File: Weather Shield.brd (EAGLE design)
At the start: 30.5 x 35.6 mm, 40 parts, among them Q1 BSS138, Q2 BSS138, U1 DS3231SN, U4 MPL3115A2LGA8, U5 HTU21D

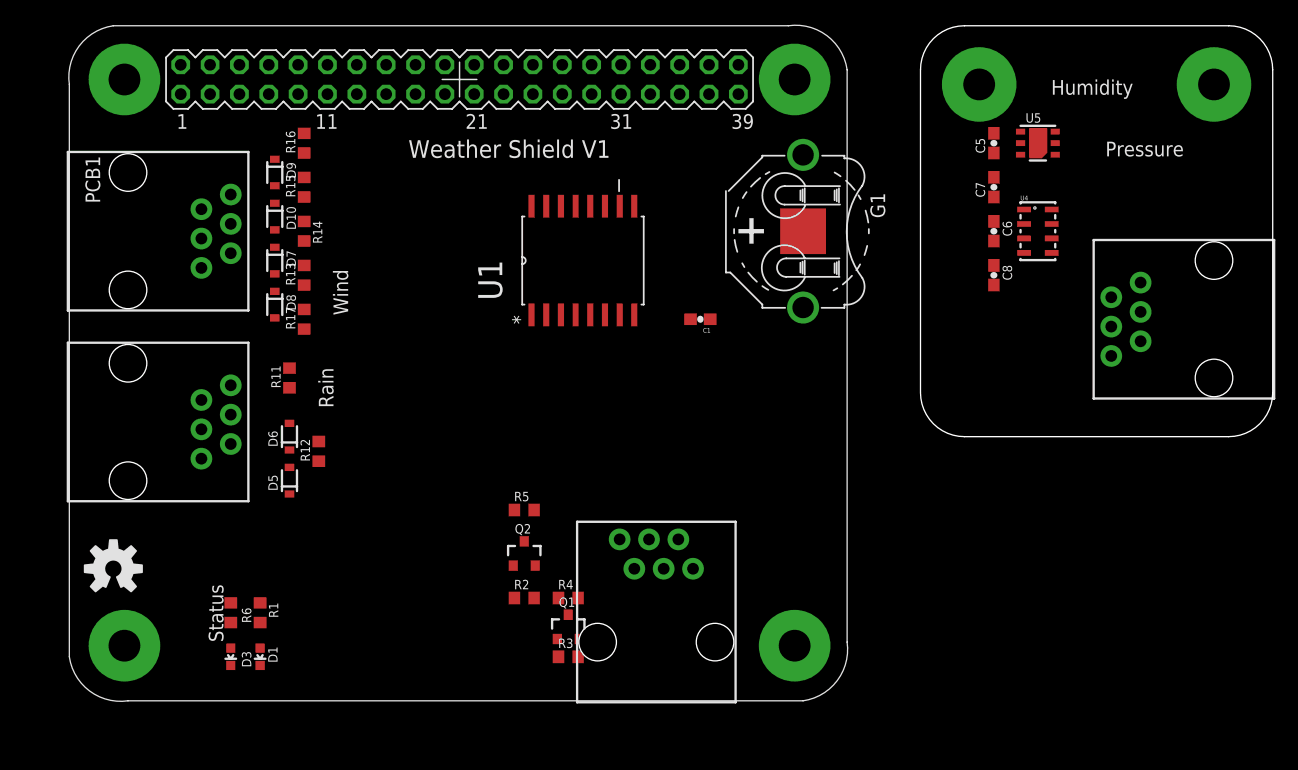
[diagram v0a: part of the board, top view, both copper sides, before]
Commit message: FSE_Weather_Shield.lbr added
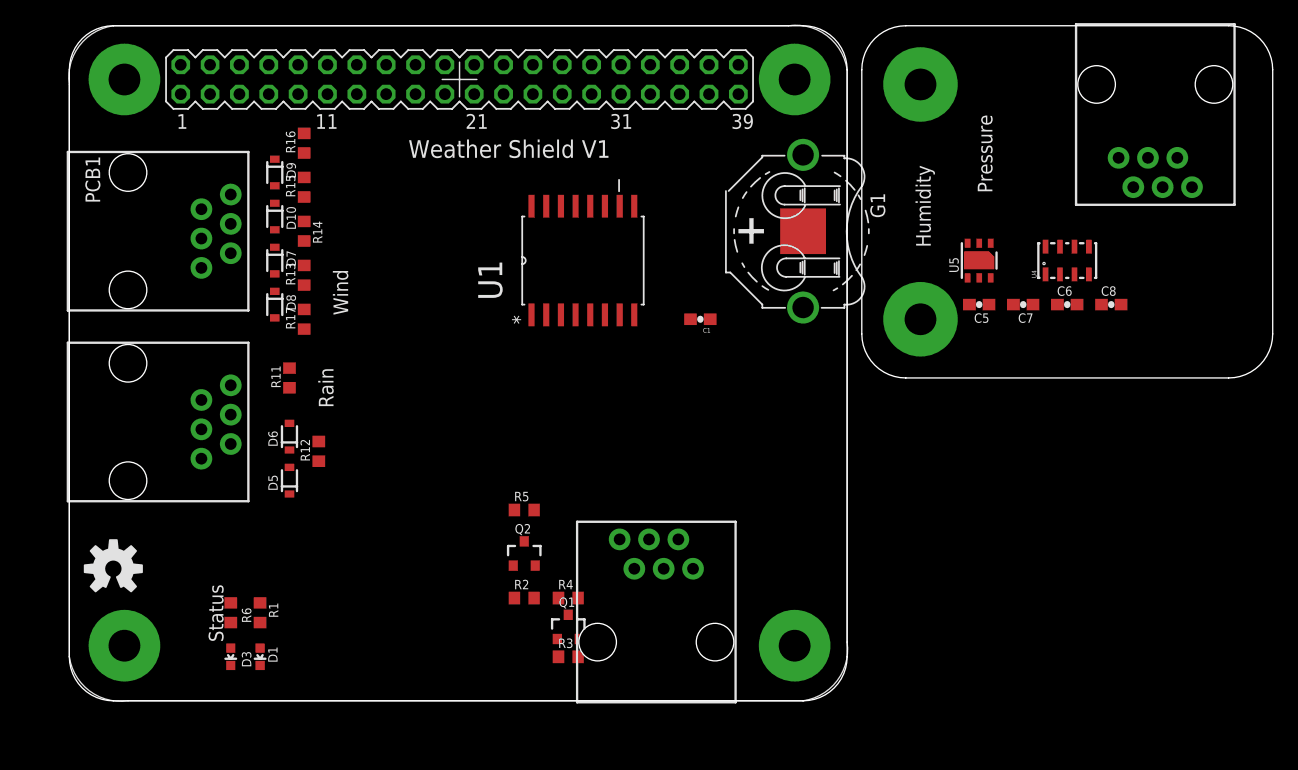
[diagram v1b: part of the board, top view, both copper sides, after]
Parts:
- moved JP9-DNP2 25.4 mm to (99.1, 53.3), turned to 180 degrees
- moved C5 14.0 mm to (78.7, 34.3), turned to 180 degrees
- moved U5 11.4 mm to (78.7, 38.1), turned to 90 degrees
- moved C7 10.5 mm to (82.5, 34.3), turned to 180 degrees
- moved C8 10.5 mm to (90.2, 34.3), turned to 0 degrees
- moved C6 8.98 mm to (86.4, 34.3), turned to 0 degrees
- moved U4 3.59 mm to (86.4, 38.1), turned to 90 degrees
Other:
- board size 30.5 x 35.6 mm -> 104.1 x 58.4 mm

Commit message: initial project version
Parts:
- added C10, C11: 1.0uF, rcl:C0603
- added C2, C9: 10uF, rcl:C0603
- added C3, C4: 47uF, SparkFun-Capacitors:EIA3528
- added D11, D4: ZLLS500, SparkFun-DiscreteSemi:SOT23
- added J7, J8: M023.5MM, SparkFun-Connectors:SCREWTERMINAL-3.5MM-2
- added JP1: (no value), SparkFun-Passives:SJ_2S
- added JP2: (no value), SparkFun-Passives:SJ_2S-NO
- added JP3: JUMPER-PTH-2-NC, SparkFun-Passives:PTH-JUMPER-NC_BOTTOM_NO_SILK
- added L1: 68uH, SparkFun-Passives:CR75
- added R10: 24k, rcl:R0603
- added R20: 220k, rcl:R0603
- added R21, R23: not fitted, rcl:R0603
- added R22: 10k, pot:S64Y
- added R8: 0.2, rcl:R0603
- added R9: 9.1k, rcl:R0603
- added TP1: SET, testpad:B1,27
- added U$1, U$2, U$3: DEAN_CONNECTOR, FSE_Weather_Shield:DEAN_CONNECTOR
- added U2: LT3652, SparkFun-PowerIC:MSOP-12_GND
- C1, C5, C6, C7, C8: device SparkFun:0603-CAP -> rcl:C0603
- moved D2 76.5 mm to (58.4, 8.89)
- moved R7 72.7 mm to (58.4, 5.08), turned to 90 degrees
- moved Q1 42.2 mm to (38.1, 48.3)
- moved R4 40.7 mm to (33.0, 48.3)
- moved R2 40.4 mm to (30.5, 48.3)
- moved D1 39.7 mm to (55.9, 8.89)
- moved D3 39.7 mm to (53.3, 8.89), turned to 0 degrees
- moved R1 39.5 mm to (55.9, 5.08)
- moved R6 39.5 mm to (53.3, 5.08)
- moved R3 37.2 mm to (38.1, 40.6)
- moved Q2 34.9 mm to (27.9, 45.7)
- moved R5 29.6 mm to (34.3, 45.7)
- moved JP9-DNP1 18.8 mm to (62.2, 14.0), turned to 90 degrees
- moved U4 10.2 mm to (96.5, 38.1)
- moved C6 8.89 mm to (95.2, 34.3)
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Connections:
- removed net STAT1: R1.1
- removed net STAT2: R6.1
- new net !CHRG: D3.C, U2.4
- new net !FAULT: D1.C, U2.5
- new net BOOST: C10.1, D11.3, U2.11
- new net FB: R10.1, R20.2, R9.2
- new net N$14: J7.2, J8.1, JP1.1, U$1.2, U$2.1
- new net N$15: R20.1, U2.7
- new net N$16: C3.A, C4.A, C9.1, D11.1, JP3.1, R10.2, R21.2, R23.2, R8.2, U2.9
- new net SENSE: L1.P$2, R21.1, R23.1, R8.1, U2.10
- new net SET: R22.S, TP1.TP, U2.2
- new net SFSASDF: J7.1, JP2.1, U$1.1
- new net SW: C10.2, D4.3, L1.P$1, U2.12
- new net TIMER: C11.2, U2.6
- new net VIN: C2.1, JP1.2, JP2.2, R22.E, U2.1, U2.3
- new net V_BATT: JP3.2, R1.1, R6.1, U$3.1
- net GND: now also C11.1, C2.2, C3.C, C4.C, C9.2, D4.1, J8.2, R22.A, R9.1, U$2.2, U$3.2, U2.13; no longer D1.C, D3.C
